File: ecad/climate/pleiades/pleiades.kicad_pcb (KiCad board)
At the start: 2 copper layers, 80 x 45 mm, 148 parts, among them J1 MCV 1,5/ 2-G-3,5, J10 47053-1000, J11 47053-1000, J2 MCV 1,5/ 2-G-3,5, J3 MCV 1,5/ 2-G-3,5, J4 M20-8760342, J5 47053-1000, J6 47053-1000, J7 215079-8, J8 640454-2, J9 640454-2, Q1 PMV45EN, Q2 PMV45EN, SW1 1825910-6, U1 LP3985IM5-3.3/NOPB, U2 AT90CAN128-16AU, U3 MCP2561-E/SN, U4 MIC4680YM, U5 TCA9544A, U6 EMC2302-1-AIZL-TR, U61 EMC2302-1-AIZL-TR, X1 32.768kHz, X2 32.768kHz, Y1 16MHz

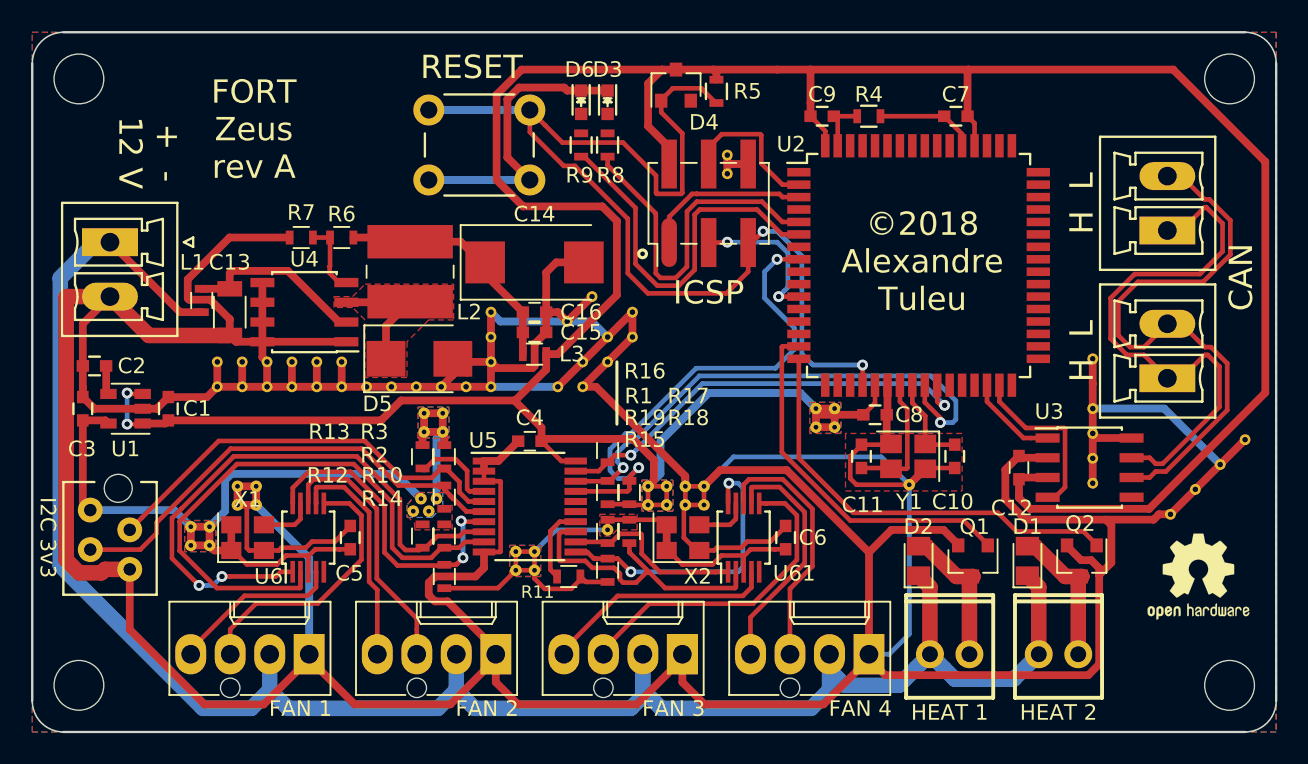
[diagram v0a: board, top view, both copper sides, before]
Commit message: Makes Pleiades KiCad 5 compatible
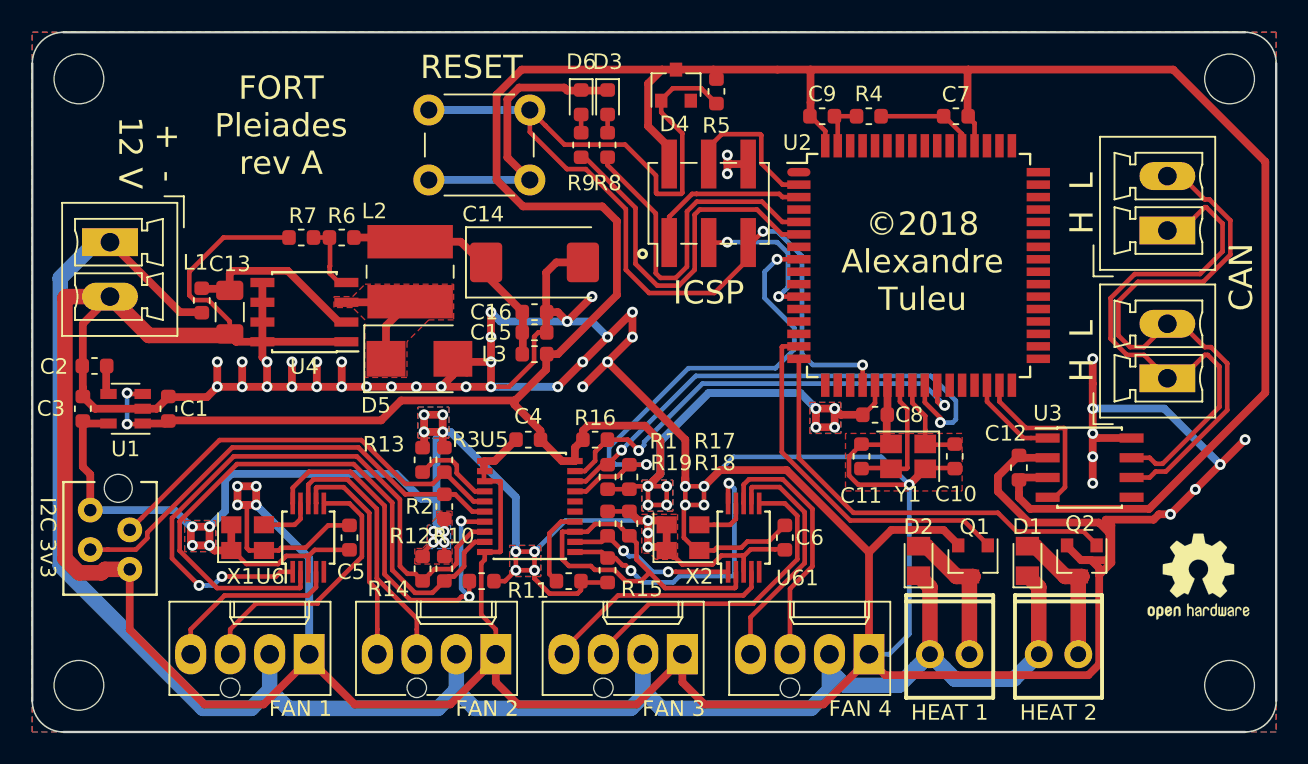
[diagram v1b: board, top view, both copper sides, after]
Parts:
- removed the REF** at (137.0, 137.0)
- removed the REF** at (174.8, 134.4)
- removed the REF** at (178.0, 131.2)
- removed the REF** at (173.2, 136.0)
- removed the REF** at (176.4, 132.8)
- removed the REF** at (168.2, 126.0)
- removed the REF** at (168.2, 129.2)
- removed the REF** at (168.2, 130.8)
- removed the REF** at (168.2, 132.4)
- removed the REF** at (168.2, 134.0)
- removed the REF** at (134.4, 123.6)
- removed the REF** at (132.3, 139.6)
- removed the REF** at (136.0, 122.0)
- removed the REF** at (138.6, 123.0)
- removed the REF** at (138.6, 124.6)
- removed the REF** at (137.0, 124.6)
- removed the REF** at (137.0, 126.2)
- removed the REF** at (135.4, 126.2)
- removed the REF** at (135.4, 127.8)
- removed the REF** at (133.8, 127.8)
- removed the REF** at (129.5, 123.0)
- removed the REF** at (129.5, 124.6)
- removed the REF** at (131.1, 139.6)
- removed the REF** at (129.5, 126.2)
- removed the REF** at (119.9, 126.2)
- removed the REF** at (118.3, 126.2)
- removed the REF** at (116.7, 126.2)
- removed the REF** at (115.1, 126.2)
- removed the REF** at (113.5, 126.2)
- removed the REF** at (111.9, 126.2)
- removed the REF** at (129.5, 127.8)
- removed the REF** at (127.9, 127.8)
- removed the REF** at (126.3, 127.8)
- removed the REF** at (132.3, 138.4)
- removed the REF** at (124.7, 127.8)
- removed the REF** at (123.1, 127.8)
- removed the REF** at (121.5, 127.8)
- removed the REF** at (119.9, 127.8)
- removed the REF** at (118.3, 127.8)
- removed the REF** at (116.7, 127.8)
- removed the REF** at (115.1, 127.8)
- removed the REF** at (113.5, 127.8)
- removed the REF** at (142.0, 135.4)
- removed the REF** at (143.2, 135.4)
- removed the REF** at (131.1, 138.4)
- removed the REF** at (143.2, 134.2)
- removed the REF** at (144.7, 114.1)
- removed the REF** at (144.7, 112.9)
- removed the REF** at (150.4, 130.4)
- removed the REF** at (151.6, 130.4)
- removed the REF** at (151.6, 129.2)
- removed the REF** at (150.4, 129.2)
- removed the REF** at (139.6, 134.2)
- removed the REF** at (140.8, 134.2)
- removed the REF** at (140.8, 135.4)
- removed the REF** at (114.4, 135.4)
- removed the REF** at (139.6, 135.4)
- removed the REF** at (156.4, 134.1)
- removed the REF** at (126.0, 135.0)
- removed the REF** at (125.0, 135.0)
- removed the REF** at (126.4, 129.5)
- removed the REF** at (125.2, 129.5)
- removed the REF** at (125.2, 130.7)
- removed the REF** at (126.4, 130.7)
- removed the REF** at (124.5, 135.8)
- removed the REF** at (125.5, 135.8)
- removed the REF** at (113.2, 135.4)
- removed the REF** at (142.0, 134.2)
- removed the REF** at (111.4, 138.0)
- removed the REF** at (110.2, 138.0)
- removed the REF** at (111.4, 136.8)
- removed the REF** at (110.2, 136.8)
- removed the REF** at (111.9, 127.8)
- removed the REF** at (114.4, 134.2)
- removed the REF** at (113.2, 134.2)
- C1, C10, C11, C12, C15, C16, C2, C3, C4, C5, C6, C7, C8, C9: footprint Capacitors_SMD:C_0603 -> Capacitor_SMD:C_0603_1608Metric
- C13: footprint Capacitors_SMD:C_1206 -> Capacitor_SMD:C_1206_3216Metric
- C14: footprint Capacitors_Tantalum_SMD:CP_Tantalum_Case-D_EIA-7343-31_Reflow -> Capacitor_Tantalum_SMD:CP_EIA-7343-31_Kemet-D
- D1, D2: footprint Diodes_SMD:D_MicroMELF -> Diode_SMD:D_MicroMELF
- D3, D6: footprint LEDs:LED_0603 -> LED_SMD:LED_0603_1608Metric
- D5: footprint Diodes_SMD:D_SMB -> Diode_SMD:D_SMB
- J1, J2, J3: footprint Connectors_Phoenix:PhoenixContact_MCV-G_02x3.50mm_Vertical -> Connector_Phoenix_MC:PhoenixContact_MCV_1,5_2-G-3.5_1x02_P3.50mm_Vertical
- J4: footprint Pin_Headers:Pin_Header_Straight_2x03_Pitch2.54mm_SMD -> Connector_PinHeader_2.54mm:PinHeader_2x03_P2.54mm_Vertical_SMD
- L1, L3, R1, R10, R11, R12, R13, R14, R15, R16, R17, R18, R19, R2, R3, R4, R5, R6, R7, R8, R9: footprint Resistors_SMD:R_0603 -> Resistor_SMD:R_0603_1608Metric
- L2: footprint Inductors_SMD:L_Wuerth_WE-PD2-Typ-MS -> Inductor_SMD:L_Wuerth_WE-PD2-Typ-MS
- Q1, Q2: footprint TO_SOT_Packages_SMD:SOT-23 -> Package_TO_SOT_SMD:SOT-23
- SW1: footprint Buttons_Switches_THT:SW_PUSH_6mm -> Button_Switch_THT:SW_PUSH_6mm
- U1: footprint TO_SOT_Packages_SMD:SOT-23-5 -> Package_TO_SOT_SMD:SOT-23-5
- U2: footprint Housings_QFP:TQFP-64_14x14mm_Pitch0.8mm -> Package_QFP:TQFP-64_14x14mm_P0.8mm
- U3, U4: footprint Housings_SOIC:SOIC-8_3.9x4.9mm_Pitch1.27mm -> Package_SO:SOIC-8_3.9x4.9mm_P1.27mm
- U5: footprint Housings_SSOP:TSSOP-20_4.4x6.5mm_Pitch0.65mm -> Package_SO:SSOP-20_4.4x6.5mm_P0.65mm
- U6, U61: footprint Housings_SSOP:MSOP-10_3x3mm_Pitch0.5mm -> Package_SO:MSOP-10_3x3mm_P0.5mm
- X1, X2: footprint Oscillators:Oscillator_SMD_Abracon_ASE-4pin_3.2x2.5mm -> Oscillator:Oscillator_SMD_Abracon_ASE-4Pin_3.2x2.5mm
- Y1: footprint Crystals:Crystal_SMD_SeikoEpson_FA238-4pin_3.2x2.5mm -> Crystal:Crystal_SMD_SeikoEpson_FA238-4Pin_3.2x2.5mm
- moved R14 2.42 mm to (128.9, 140.3), turned to 0 degrees
- moved R10 2.10 mm to (126.5, 139.5)
- moved R12 2.10 mm to (125.1, 139.5)
- moved R16 1.06 mm to (136.2, 131.2), turned to 180 degrees
- moved R1 1.00 mm to (137.0, 133.6)
- moved R17 1.00 mm to (138.4, 133.6)
- moved R2 0.60 mm to (126.5, 135.5)
- moved R18 0.50 mm to (138.4, 136.6)
- moved R19 0.50 mm to (137.0, 136.6)
- moved R11 0.30 mm to (134.5, 140.3)
- moved R13 0.20 mm to (125.1, 132.5)
- moved R3 0.20 mm to (126.5, 132.5)
- moved C4 0.14 mm to (131.9, 131.2)
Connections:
- J10 pad 4: Net-(J10-Pad4) -> /Fan PWM Controller 2/PWM1
- U2 pad 1: (no net) -> Net-(U2-Pad1)
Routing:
- net +3V3: track 98.1 -> 119.3 mm, vias 0 -> 19
- net /Fan PWM Controller 1/~ALERT: track 20.7 -> 26.4 mm
- net /Fan PWM Controller 2/PWM1: track 9.84 -> 15.4 mm
- net Net-(J10-Pad4): track 5.54 -> 0.00 mm
- net /Fan PWM Controller 2/SCL: track 19.1 -> 22.9 mm
- net /Fan PWM Controller 1/SCL: track 37.4 -> 40.7 mm
- net GND: track 463.0 -> 466.1 mm, vias 0 -> 50
- net /Fan PWM Controller 1/SDA: track 37.9 -> 41.0 mm
- net /I2C Multiplexer/SCL_5V: track 34.5 -> 33.1 mm
- net Net-(D6-Pad2): track 0.00 -> 1.18 mm
- net Net-(D3-Pad2): track 0.00 -> 1.18 mm
- net /I2C Multiplexer/SDA_5V: track 28.5 -> 29.3 mm
- net /Fan PWM Controller 2/SDA: track 11.8 -> 11.0 mm, vias 0 -> 2
- net /Fan PWM Controller 1/PWM1: track 11.0 -> 11.8 mm
- net +5V: track 213.7 -> 214.4 mm, vias 2 -> 10
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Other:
- net class Default: clearance 0.195 -> 0.175
- net class Power: clearance 0.195 -> 0.175
- rule trace_clearance: 0.195 -> 0.175
- board text added: "FORT Pleiades rev A"
- board text removed: "FORT Zeus rev A"
